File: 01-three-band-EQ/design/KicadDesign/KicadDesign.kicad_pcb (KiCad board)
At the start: 2 copper layers, 90 x 70 mm, 29 parts, among them J1 Supply, J2 Output, J3 Input, U1 TL072, U2 TL072, U3 TL072

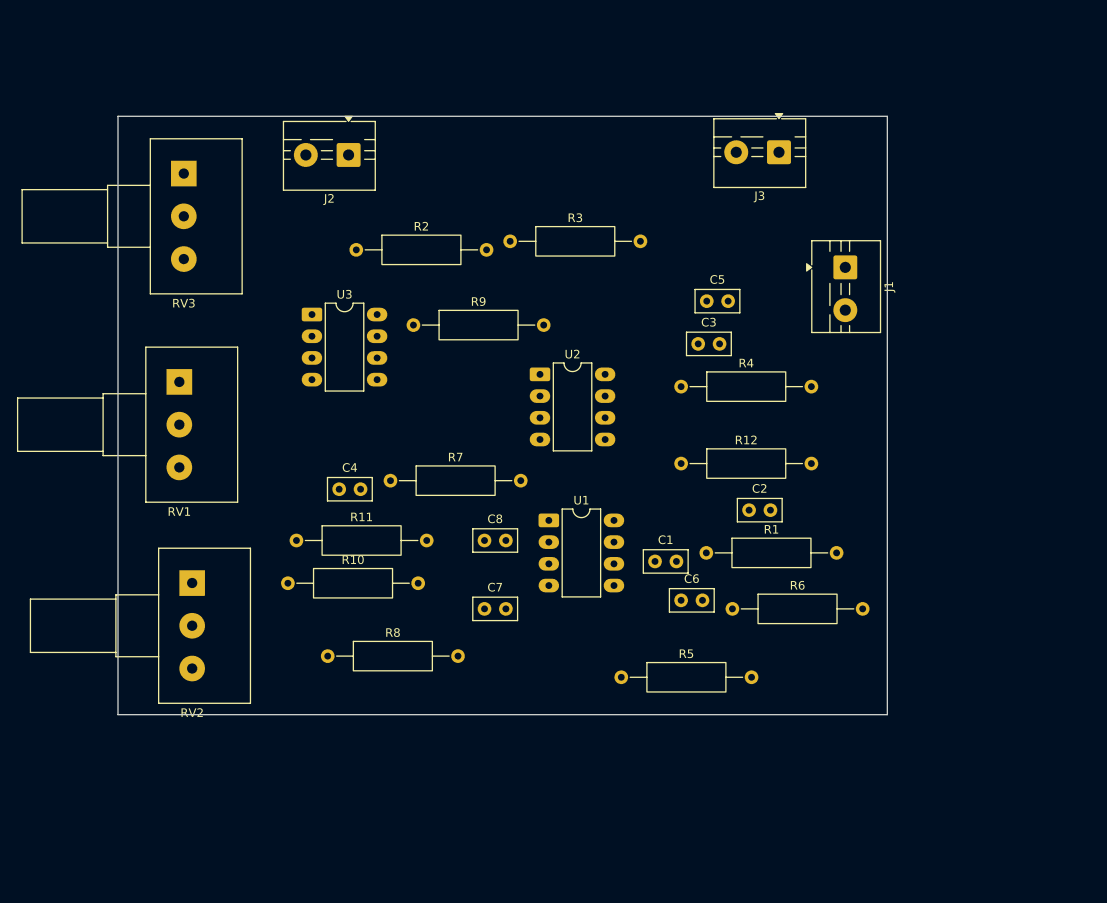
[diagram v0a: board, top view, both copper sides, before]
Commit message: Placa routeada nomas faltan 2 PINES, voy a seguir intentando pero si no con cables
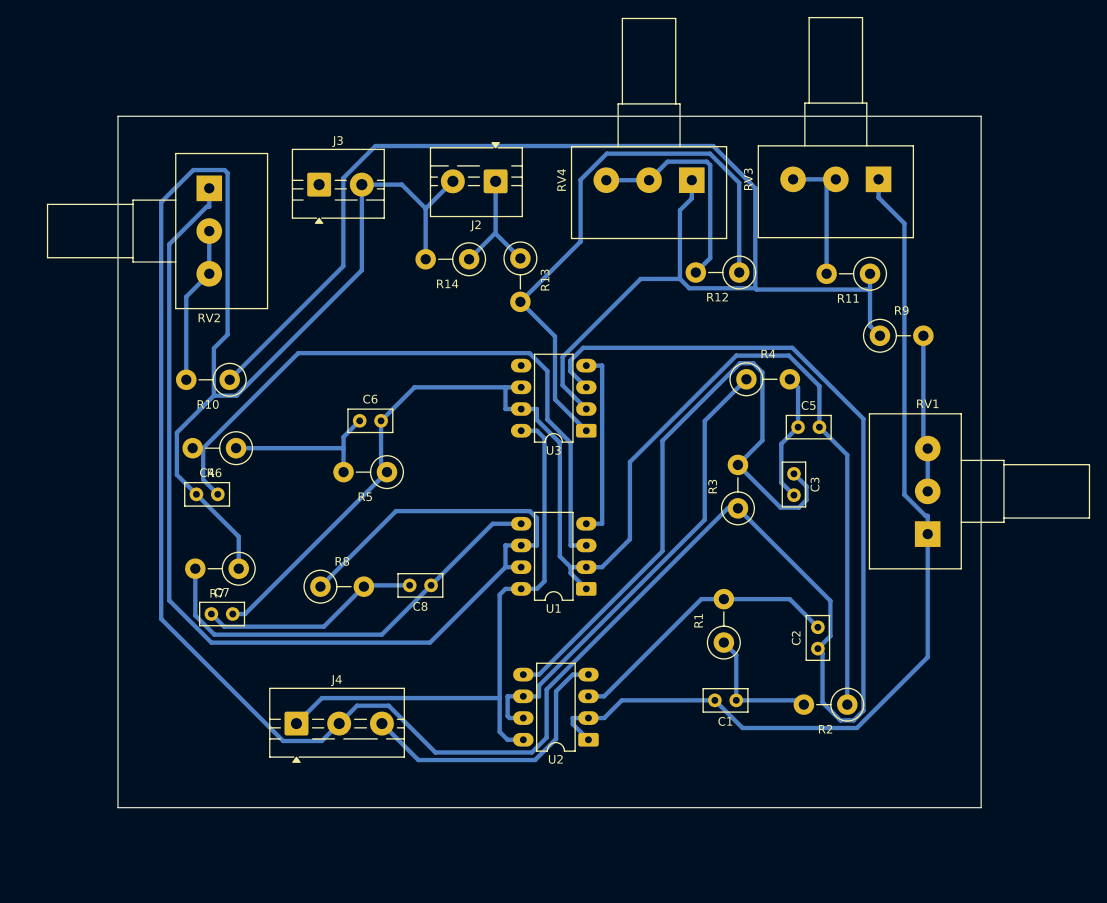
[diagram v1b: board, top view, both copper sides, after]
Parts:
- removed J1: Supply, TerminalBlock:TerminalBlock_MaiXu_MX126-5.0-02P_1x02_P5.00mm
- added J4: Supply, TerminalBlock:TerminalBlock_MaiXu_MX126-5.0-03P_1x03_P5.00mm, F.Cu at (51.0, 98.4)
- added R13: 12k, Resistor_THT:R_Axial_DIN0411_L9.9mm_D3.6mm_P5.08mm_Vertical, F.Cu at (77.2, 44.0)
- added R14: 1k, Resistor_THT:R_Axial_DIN0411_L9.9mm_D3.6mm_P5.08mm_Vertical, F.Cu at (71.2, 44.1)
- added RV4: 1k, Potentiometer_THT:Potentiometer_Alps_RK163_Single_Horizontal, F.Cu at (97.2, 34.9)
- R1, R10, R11, R2, R3, R4, R5, R6, R7, R8, R9: footprint Resistor_THT:R_Axial_DIN0309_L9.0mm_D3.2mm_P15.24mm_Horizontal -> Resistor_THT:R_Axial_DIN0411_L9.9mm_D3.6mm_P5.08mm_Vertical
- R12: value 2.7k -> 1.5k; footprint Resistor_THT:R_Axial_DIN0309_L9.0mm_D3.2mm_P15.24mm_Horizontal -> Resistor_THT:R_Axial_DIN0411_L9.9mm_D3.6mm_P5.08mm_Vertical
- moved RV1 89.3 mm to (124.8, 76.2), turned to 180 degrees
- moved RV3 81.3 mm to (119.1, 34.8), turned to -90 degrees
- moved R2 78.3 mm to (115.4, 96.2), turned to 180 degrees
- moved R11 74.0 mm to (118.1, 45.8), turned to 180 degrees
- moved R6 61.0 mm to (43.9, 66.2), turned to 180 degrees
- moved R9 54.6 mm to (119.3, 53.0)
- moved J3 53.9 mm to (53.6, 35.4), turned to 0 degrees
- moved RV2 46.2 mm to (40.8, 35.8)
- moved U2 43.1 mm to (85.2, 100.3), turned to 180 degrees
- moved C6 43.1 mm to (58.4, 63.0)
- moved R3 41.1 mm to (102.7, 73.2), turned to 90 degrees
- moved R5 36.4 mm to (61.6, 69.0), turned to 180 degrees
- moved U3 34.9 mm to (84.9, 64.2), turned to 180 degrees
- moved C7 32.0 mm to (41.0, 85.6)
- moved R10 24.8 mm to (43.2, 58.2), turned to 180 degrees
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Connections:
- J3 pad 1: /IN -> /INPUT
- R12 pad 1: /Out -> Net-(R12-Pad1)
- R12 pad 2: Net-(U3A--) -> Net-(R12-Pad2)
- U3 pad 1: /Out -> Net-(R12-Pad1)
- U3 pad 5: (no net) -> /INPUT
- U3 pad 6: (no net) -> /IN
- U3 pad 7: (no net) -> /IN
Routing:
- net GND: track 0.00 -> 365.5 mm
- net /IN: track 0.00 -> 163.6 mm
- net Net-(U3A--): track 0.00 -> 160.0 mm
- net /OUT_BP: track 0.00 -> 135.9 mm
- net /OUT_LP: track 0.00 -> 108.9 mm
- net Net-(U2B-+): track 0.00 -> 77.2 mm
- net Net-(U1A-+): track 0.00 -> 76.4 mm
- net VCC: track 0.00 -> 69.9 mm
- net Net-(R12-Pad1): track 0.00 -> 67.2 mm
- net VEE: track 0.00 -> 55.5 mm
- net /OUT_HP: track 0.00 -> 55.1 mm
- net Net-(U1B-+): track 0.00 -> 49.9 mm
- net Net-(U2A-+): track 0.00 -> 32.9 mm
- net Net-(R12-Pad2): track 0.00 -> 26.5 mm
- net Net-(C7-Pad1): track 0.00 -> 25.8 mm
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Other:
- board size 90 x 70 mm -> 101 x 80.9 mm

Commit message: Placa routeada porfavor checar
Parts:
- added R15: 0, Resistor_THT:R_Axial_DIN0411_L9.9mm_D3.6mm_P5.08mm_Vertical, F.Cu at (70.3, 103.2)
- added R16: 270k, Resistor_THT:R_Axial_DIN0207_L6.3mm_D2.5mm_P15.24mm_Horizontal, F.Cu at (77.7, 87.5)
- moved U3 11.5 mm to (73.8, 61.2)
- moved C6 2.82 mm to (57.3, 65.6)
- moved R5 2.82 mm to (60.5, 71.6)
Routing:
- net GND: track 365.5 -> 433.4 mm
- net VEE: track 55.5 -> 103.6 mm
- net /OUT_BP: track 135.9 -> 103.6 mm
- net Net-(U1A-+): track 76.4 -> 106.7 mm
- net Net-(R12-Pad1): track 67.2 -> 40.8 mm
- net /INPUT: track 0.00 -> 24.5 mm
- net Net-(U3A--): track 160.0 -> 139.1 mm
- net VCC: track 69.9 -> 85.3 mm
- net Net-(C7-Pad1): track 25.8 -> 36.7 mm
- net Net-(U2B-+): track 77.2 -> 88.0 mm
- net /IN: track 163.6 -> 172.2 mm
- net Net-(R12-Pad2): track 26.5 -> 18.1 mm
- net Net-(C3-Pad2): track 15.4 -> 20.7 mm
- net Net-(U1B-+): track 49.9 -> 44.9 mm

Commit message: feat: PCB routed
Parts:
- removed R15: 0, Resistor_THT:R_Axial_DIN0411_L9.9mm_D3.6mm_P5.08mm_Vertical
- removed R16: 270k, Resistor_THT:R_Axial_DIN0207_L6.3mm_D2.5mm_P15.24mm_Horizontal
- C7: footprint Capacitor_THT:C_Disc_D5.0mm_W2.5mm_P2.50mm -> Capacitor_THT:C_Disc_D8.0mm_W5.0mm_P7.50mm
- R1, R3: footprint Resistor_THT:R_Axial_DIN0411_L9.9mm_D3.6mm_P5.08mm_Vertical -> Resistor_THT:R_Axial_DIN0411_L9.9mm_D3.6mm_P12.70mm_Horizontal
- moved RV1 91.9 mm to (35.7, 98.5), turned to 90 degrees
- moved R9 83.7 mm to (52.4, 103.5), turned to 90 degrees
- moved R2 83.1 mm to (39.7, 61.9), turned to -90 degrees
- moved RV3 72.6 mm to (84.4, 98.5), turned to 90 degrees
- moved R1 69.8 mm to (31.4, 83.3), turned to 0 degrees
- moved C1 67.8 mm to (39.6, 70.3), turned to 0 degrees
- moved RV2 65.4 mm to (59.4, 98.5), turned to 90 degrees
- moved RV4 64.7 mm to (109.1, 98.5), turned to 90 degrees
- moved C2 63.8 mm to (48.4, 84.7)
- moved J4 60.3 mm to (91.2, 53.5)
- moved R11 60.0 mm to (101.5, 103.5), turned to 90 degrees
- moved R6 59.4 mm to (103.2, 69.7)
- moved J3 59.2 mm to (109.8, 54.1)
- moved R14 58.4 mm to (126.8, 61.7)
- moved R3 57.8 mm to (46.9, 88.4), turned to 0 degrees
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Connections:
- RV3 pad 1: /OUT_LP -> /OUT_HP
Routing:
- net GND: track 433.4 -> 209.0 mm
- net Net-(U1A-+): track 106.7 -> 21.6 mm
- net Net-(U2B-+): track 88.0 -> 17.5 mm
- net /OUT_LP: track 109.0 -> 38.9 mm
- net VEE: track 103.6 -> 163.5 mm
- net Net-(U3A--): track 139.1 -> 85.4 mm
- net VCC: track 85.3 -> 128.0 mm
- net /OUT_BP: track 103.6 -> 65.8 mm
- net /IN: track 172.2 -> 135.1 mm
- net Net-(U1B-+): track 44.9 -> 10.5 mm
- net /OUT_HP: track 55.2 -> 89.0 mm
- net Net-(R12-Pad1): track 40.8 -> 12.3 mm
- net Net-(U2A-+): track 32.9 -> 14.9 mm
- net Net-(C7-Pad1): track 36.7 -> 21.4 mm
- net Net-(C3-Pad2): track 20.7 -> 8.83 mm
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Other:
- board size 101 x 80.9 mm -> 101.4 x 61.6 mm

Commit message: feat: PCB routed
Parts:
- moved R14 9.26 mm to (117.8, 59.6)
- moved J2 8.89 mm to (117.8, 52.2)
- moved R2 6.50 mm to (39.2, 68.4), turned to -135 degrees
- moved C1 4.99 mm to (38.9, 75.2), turned to 45 degrees
- moved R12 4.66 mm to (119.2, 89.0), turned to 180 degrees
- moved R8 4.66 mm to (76.7, 83.2)
- moved R7 4.63 mm to (71.4, 64.0)
- moved J3 4.53 mm to (105.7, 52.2), turned to 180 degrees
- moved R6 4.16 mm to (99.1, 69.6)
- moved C7 3.78 mm to (80.6, 87.6)
- moved C4 3.55 mm to (86.5, 63.1)
- moved C8 3.46 mm to (71.4, 74.4)
- moved U3 3.23 mm to (112.4, 77.5)
- moved J4 2.63 mm to (93.5, 52.2), turned to 180 degrees
- moved C3 2.32 mm to (59.6, 78.1)
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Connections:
- J3 pad 1: /INPUT -> GND
- J3 pad 2: GND -> /INPUT
- J4 pad 1: VCC -> VEE
- J4 pad 3: VEE -> VCC
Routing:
- net VCC: track 128.0 -> 141.4 mm
- net /OUT_BP: track 65.8 -> 56.9 mm
- net Net-(R12-Pad1): track 12.3 -> 18.5 mm
- net Net-(C1-Pad1): track 21.9 -> 15.8 mm
- net /OUT_HP: track 89.0 -> 84.3 mm
- net /IN: track 135.1 -> 139.7 mm
- net Net-(U1A-+): track 21.6 -> 17.5 mm
- net Net-(C7-Pad1): track 21.4 -> 17.6 mm
- net GND: track 209.0 -> 205.5 mm
- net VEE: track 163.5 -> 166.5 mm
- net /INPUT: track 16.6 -> 19.4 mm
- net /OUT_LP: track 38.9 -> 41.4 mm
- net Net-(U2B-+): track 17.5 -> 15.2 mm
- net Net-(U1B-+): track 10.5 -> 12.7 mm
- net Net-(C6-Pad1): track 13.1 -> 11.6 mm
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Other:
- board size 101.4 x 61.6 mm -> 96.5 x 60 mm
